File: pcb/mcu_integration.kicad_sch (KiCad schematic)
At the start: 32 parts, among them J5 DM3BT-DSF-PEJS, U1 STM32F103RBTx, U6 LM35DM, Y1 ECS-80-18-5PX-GM-TR

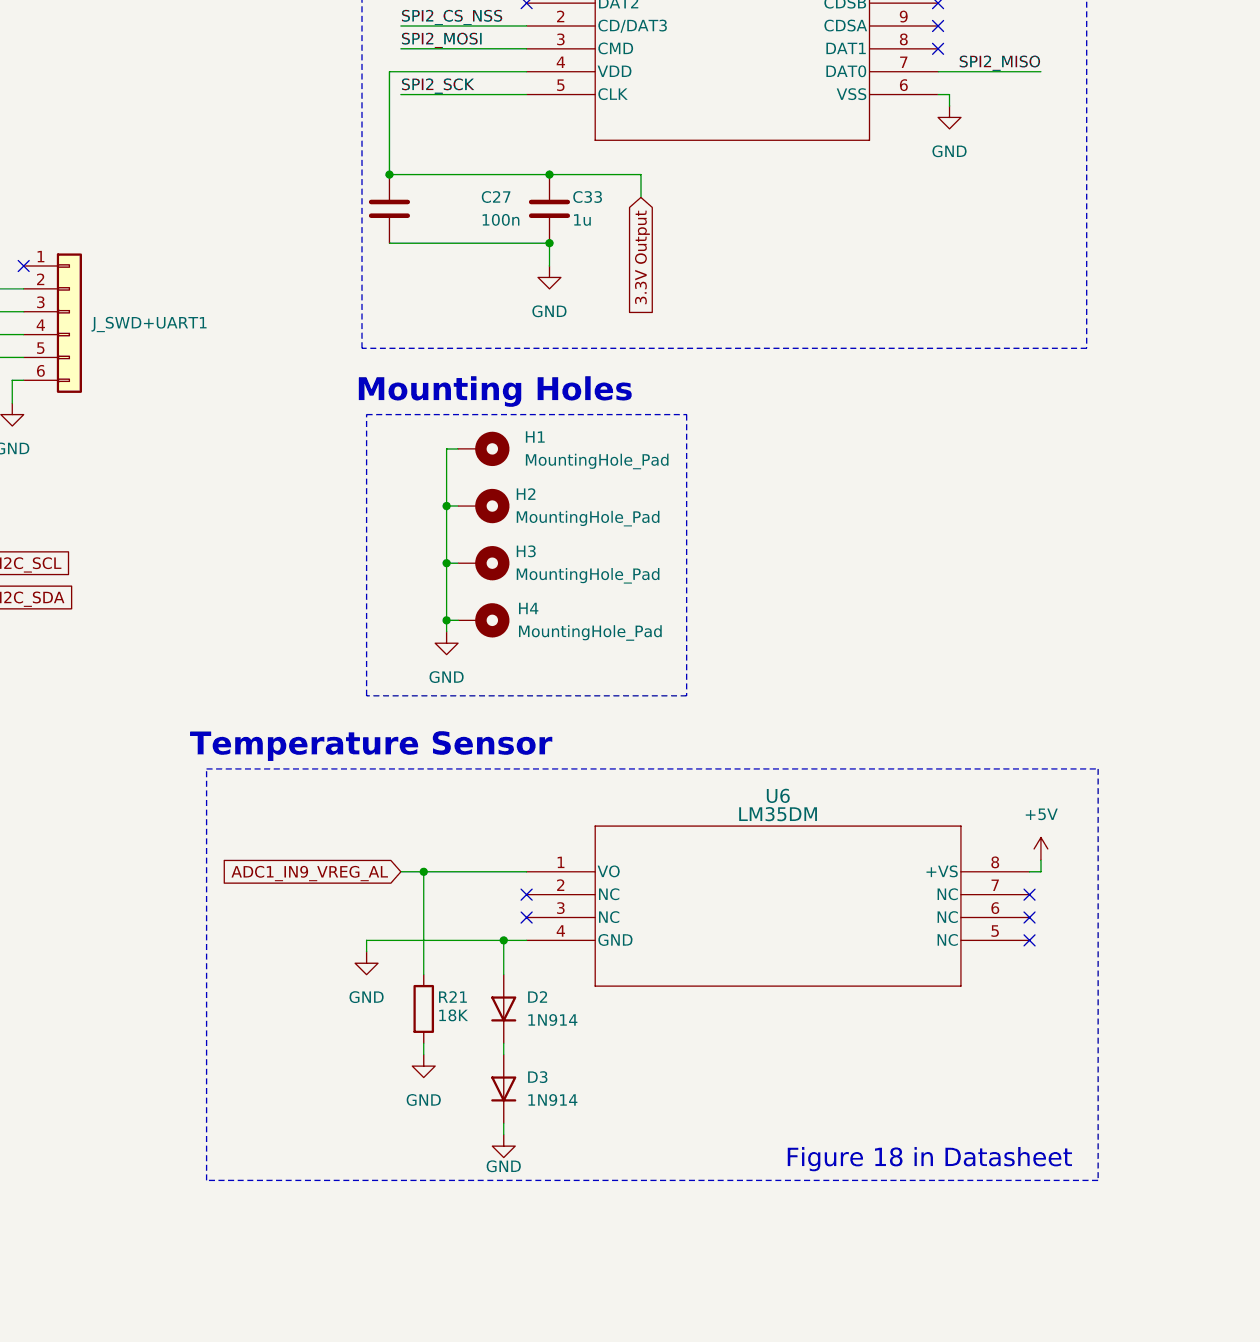
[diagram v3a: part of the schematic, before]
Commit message: Added GND and PWR planes
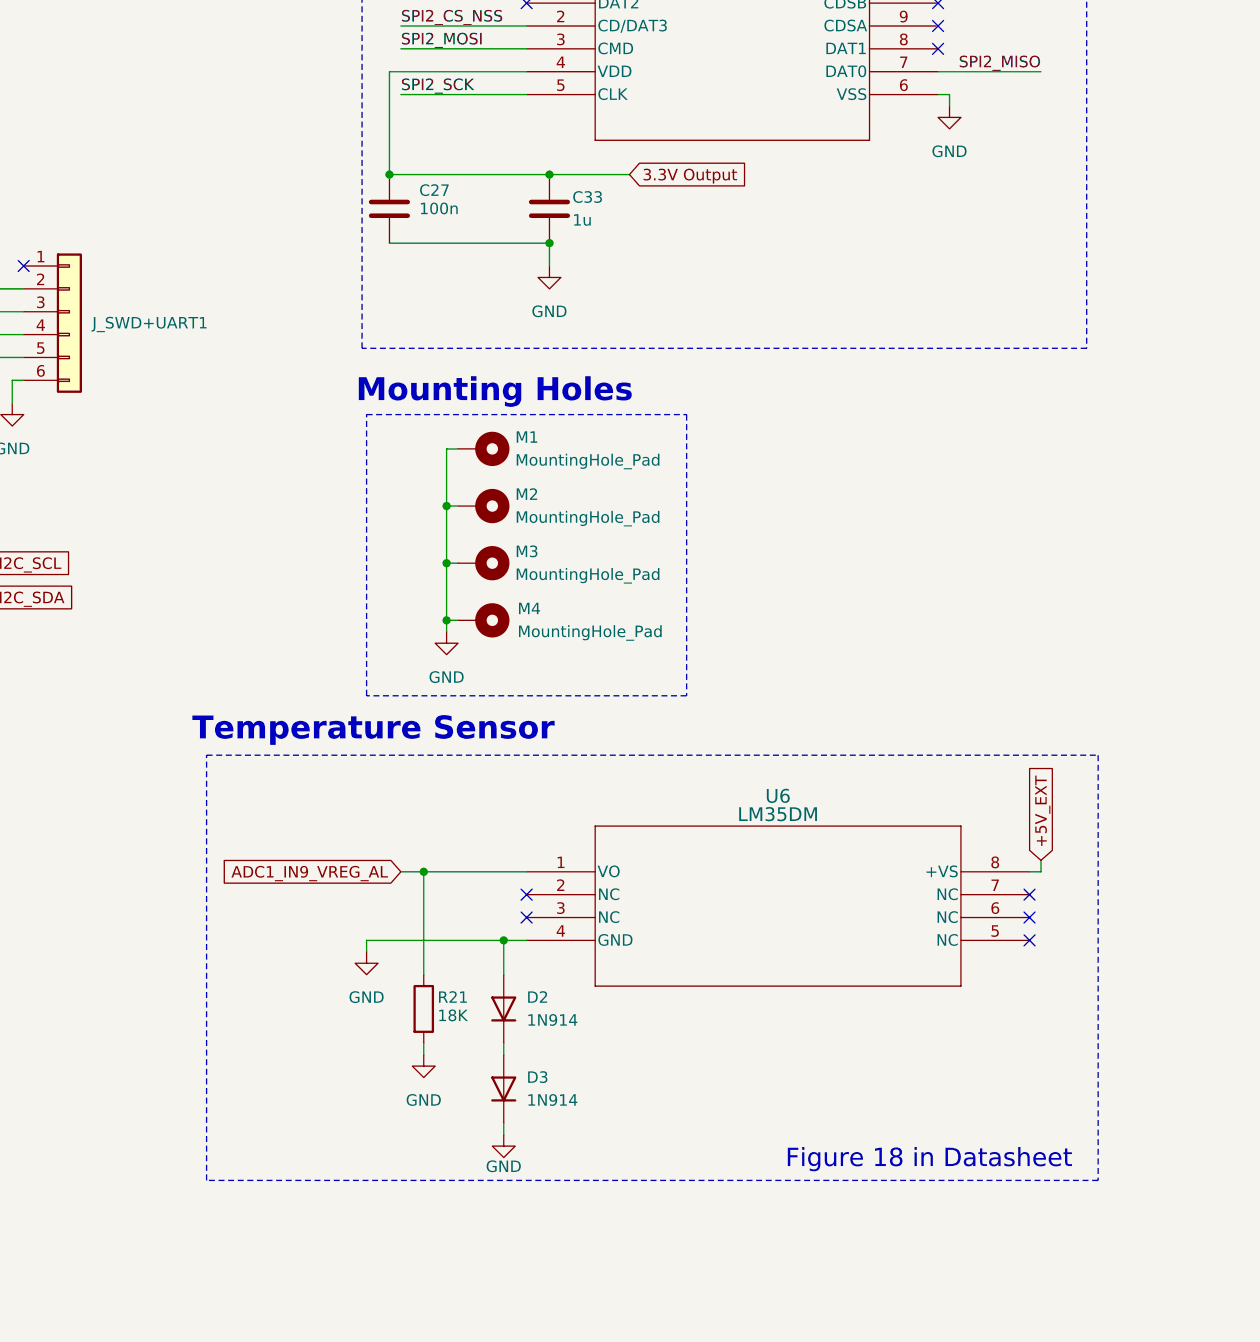
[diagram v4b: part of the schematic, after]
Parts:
- renumbered H1 to M1, H2 to M2, H3 to M3, H4 to M4
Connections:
- net +5V renamed +5V_EXT
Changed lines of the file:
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@@
 	(wire
 		(pts
-			(xy 232.41 54.61) (xy 232.41 52.07)
-		)
-		(stroke
-			(width 0)
-			(type default)
-		)
-	)
-	(wire
-		(pts
 			(xy 118.11 20.32) (xy 119.38 20.32)
 		)
@@
 	(wire
 		(pts
-			(xy 232.41 52.07) (xy 222.25 52.07)
+			(xy 231.14 52.07) (xy 222.25 52.07)
 		)
 		(stroke
@@
 	)
 	(rectangle
-		(start 184.15 118.11)
+		(start 184.15 116.586)
 		(end 283.21 163.83)
 		(stroke
@@
 	(text "Temperature Sensor"
 		(exclude_from_sim no)
-		(at 202.438 115.57 0)
+		(at 202.692 113.792 0)
 		(effects
 			(font
@@
 	(global_label "3.3V Output"
 		(shape input)
-		(at 232.41 54.61 270)
+		(at 231.14 52.07 0)
 		(fields_autoplaced yes)
 		(effects
@@
 				(size 1.27 1.27)
 			)
-			(justify right)
+			(justify left)
 		)
 		(property "Intersheetrefs" "${INTERSHEET_REFS}"
-			(at 232.41 68.9041 90)
+			(at 245.4341 52.07 0)
 			(effects
 				(font
 					(size 1.27 1.27)
 				)
-				(justify right)
+				(justify left)
 				(hide yes)
 			)
@@
 		)
 	)
+	(global_label "+5V_EXT"
+		(shape input)
+		(at 276.86 128.27 90)
+		(fields_autoplaced yes)
+		(effects
+			(font
+				(size 1.27 1.27)
+			)
+			(justify left)
+		)
+		(property "Intersheetrefs" "${INTERSHEET_REFS}"
+			(at 276.86 117.1206 90)
+			(effects
+				(font
+					(size 1.27 1.27)
+				)
+				(justify left)
+				(hide yes)
+			)
+		)
+	)
 	(global_label "ADC1_IN1_OPAMP_NOSHD"
 		(shape input)
@@
 		(on_board yes)
 		(dnp no)
-		(property "Reference" "H4"
+		(property "Reference" "M4"
 			(at 218.694 100.33 90)
 			(effects
@@
 			(project "mcu_integration"
 				(path "/c0210bc3-f67f-47d8-a34e-f002a728adb2"
-					(reference "H4")
+					(reference "M4")
 					(unit 1)
 				)
@@
 		(dnp no)
 		(fields_autoplaced yes)
-		(property "Reference" "H2"
+		(property "Reference" "M2"
 			(at 218.44 87.6299 90)
 			(effects
@@
 			(project "mcu_integration"
 				(path "/c0210bc3-f67f-47d8-a34e-f002a728adb2"
-					(reference "H2")
+					(reference "M2")
 					(unit 1)
 				)
@@
 		(dnp no)
 		(fields_autoplaced yes)
-		(property "Reference" "H3"
+		(property "Reference" "M3"
 			(at 218.44 93.9799 90)
 			(effects
@@
 			(project "mcu_integration"
 				(path "/c0210bc3-f67f-47d8-a34e-f002a728adb2"
-					(reference "H3")
+					(reference "M3")
 					(unit 1)
 				)
@@
 		(dnp no)
 		(property "Reference" "C27"
-			(at 214.63 54.61 0)
+			(at 207.772 53.848 0)
 			(effects
 				(font
@@
 		)
 		(property "Value" "100n"
-			(at 214.63 57.15 0)
+			(at 207.772 55.88 0)
 			(effects
 				(font
@@
 	)
 	(symbol
-		(lib_id "power:+5V")
-		(at 276.86 128.27 0)
-		(unit 1)
-		(exclude_from_sim no)
-		(in_bom yes)
-		(on_board yes)
-		(dnp no)
-		(fields_autoplaced yes)
-		(property "Reference" "#PWR079"
-			(at 276.86 132.08 0)
-			(effects
-				(font
-					(size 1.27 1.27)
-				)
-				(hide yes)
-			)
-		)
-		(property "Value" "+5V"
-			(at 276.86 123.19 0)
-			(effects
-				(font
-					(size 1.27 1.27)
-				)
-			)
-		)
-		(property "Footprint" ""
-			(at 276.86 128.27 0)
-			(effects
-				(font
-					(size 1.27 1.27)
-				)
-				(hide yes)
-			)
-		)
-		(property "Datasheet" ""
-			(at 276.86 128.27 0)
-			(effects
-				(font
-					(size 1.27 1.27)
-				)
-				(hide yes)
-			)
-		)
-		(property "Description" "Power symbol creates a global label with name \"+5V\""
-			(at 276.86 128.27 0)
-			(effects
-				(font
-					(size 1.27 1.27)
-				)
-				(hide yes)
-			)
-		)
-		(pin "1"
-		)
-		(instances
-			(project "mcu_integration"
-				(path "/c0210bc3-f67f-47d8-a34e-f002a728adb2"
-					(reference "#PWR079")
-					(unit 1)
-				)
-			)
-		)
-	)
-	(symbol
 		(lib_name "GND_1")
 		(lib_id "power:GND")
@@
 		(dnp no)
 		(fields_autoplaced yes)
-		(property "Reference" "H1"
-			(at 219.456 81.2799 90)
+		(property "Reference" "M1"
+			(at 218.44 81.2799 90)
 			(effects
 				(font
@@
 		)
 		(property "Value" "MountingHole_Pad"
-			(at 219.456 83.8199 90)
+			(at 218.44 83.8199 90)
 			(effects
 				(font
@@
 			(project "mcu_integration"
 				(path "/c0210bc3-f67f-47d8-a34e-f002a728adb2"
-					(reference "H1")
+					(reference "M1")
 					(unit 1)
 				)

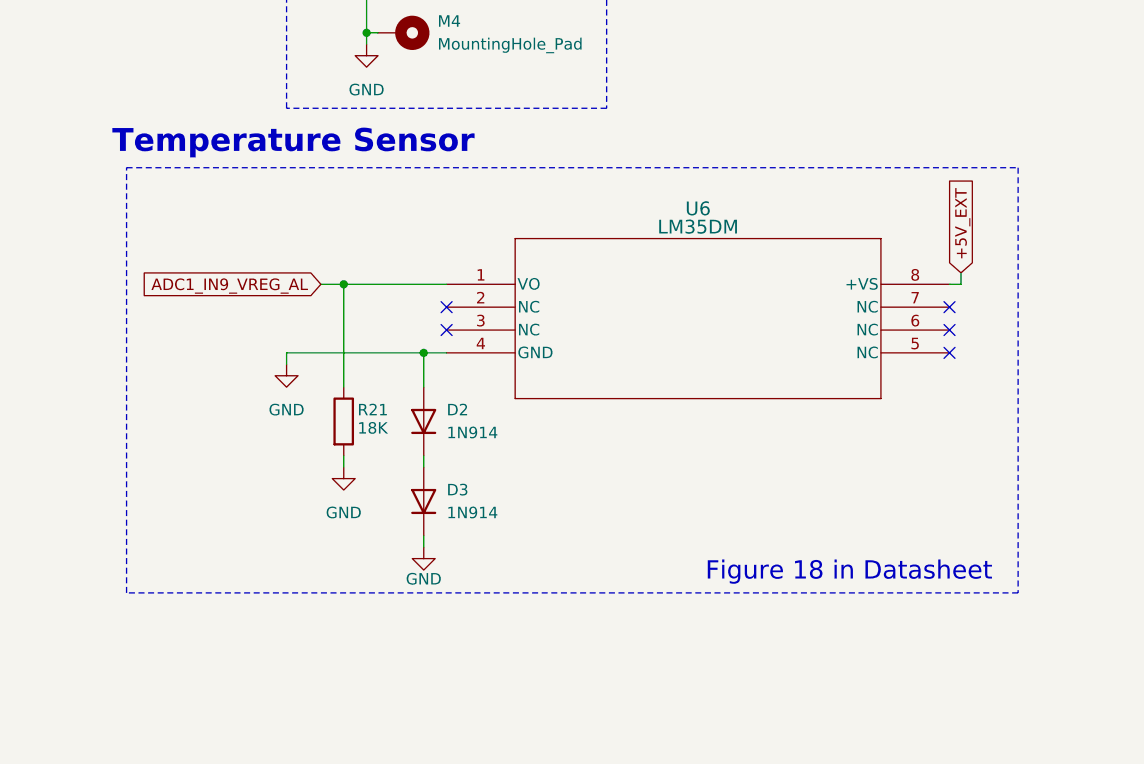
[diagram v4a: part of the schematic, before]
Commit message: Added +5v connections
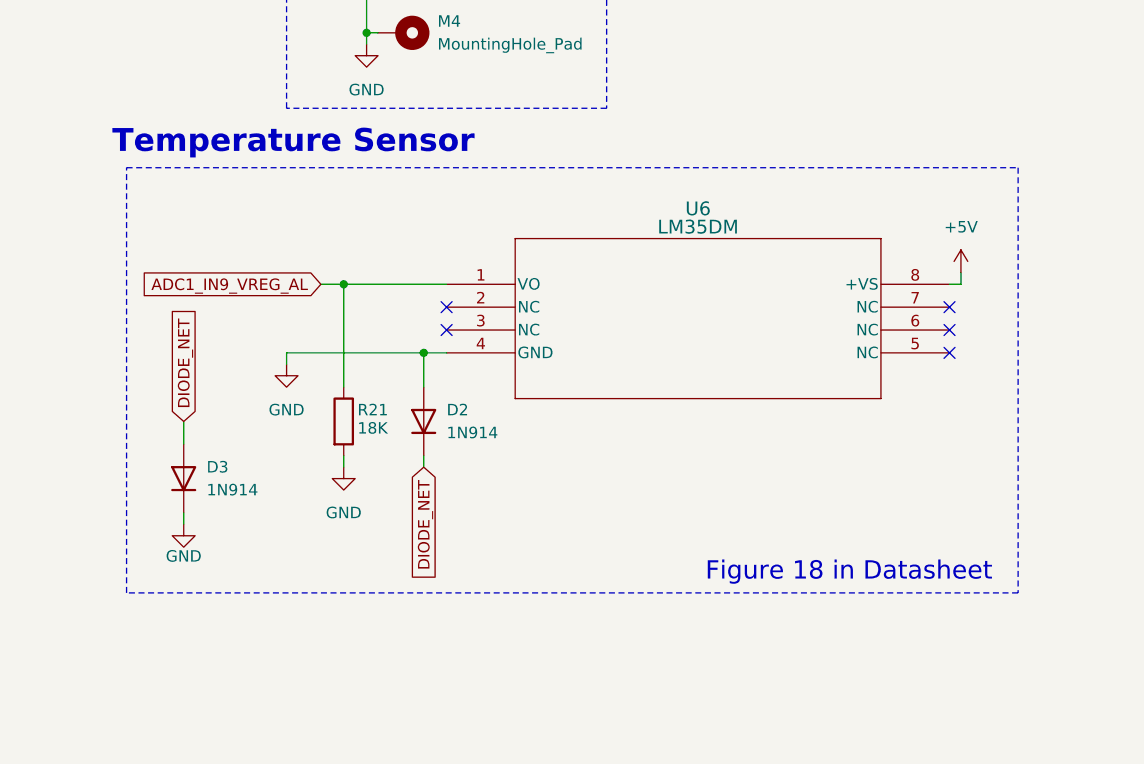
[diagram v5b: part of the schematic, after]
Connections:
- net DIODE_NET: now reaches D2.1 (K), D3.2 (A)
- net +5V_EXT renamed +5V
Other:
- moved on the sheet: D3
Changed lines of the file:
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@@
 	(wire
 		(pts
+			(xy 217.17 148.59) (xy 217.17 149.86)
+		)
+		(stroke
+			(width 0)
+			(type default)
+		)
+	)
+	(wire
+		(pts
 			(xy 106.68 21.59) (xy 118.11 21.59)
 		)
@@
 	(wire
 		(pts
+			(xy 190.5 144.78) (xy 190.5 147.32)
+		)
+		(stroke
+			(width 0)
+			(type default)
+		)
+	)
+	(wire
+		(pts
 			(xy 60.96 132.08) (xy 76.2 132.08)
 		)
@@
 	(wire
 		(pts
-			(xy 217.17 149.86) (xy 217.17 148.59)
-		)
-		(stroke
-			(width 0)
-			(type default)
-		)
-	)
-	(wire
-		(pts
 			(xy 205.74 38.1) (xy 219.71 38.1)
 		)
@@
 	(wire
 		(pts
-			(xy 217.17 157.48) (xy 217.17 158.75)
+			(xy 190.5 154.94) (xy 190.5 156.21)
 		)
 		(stroke
@@
 		)
 	)
+	(global_label "DIODE_NET"
+		(shape input)
+		(at 217.17 149.86 270)
+		(fields_autoplaced yes)
+		(effects
+			(font
+				(size 1.27 1.27)
+			)
+			(justify right)
+		)
+		(property "Intersheetrefs" "${INTERSHEET_REFS}"
+			(at 217.17 162.8842 90)
+			(effects
+				(font
+					(size 1.27 1.27)
+				)
+				(justify right)
+				(hide yes)
+			)
+		)
+	)
 	(global_label "ADC1_IN11_OPTO_E_NOSHD"
 		(shape input)
@@
 		)
 	)
-	(global_label "+5V_EXT"
+	(global_label "ADC1_IN1_OPAMP_NOSHD"
 		(shape input)
-		(at 276.86 128.27 90)
+		(at 127 39.37 0)
 		(fields_autoplaced yes)
 		(effects
@@
 		)
 		(property "Intersheetrefs" "${INTERSHEET_REFS}"
-			(at 276.86 117.1206 90)
+			(at 153.7524 39.37 0)
 			(effects
 				(font
@@
 		)
 	)
-	(global_label "ADC1_IN1_OPAMP_NOSHD"
+	(global_label "OBC_I2C_SCL"
 		(shape input)
-		(at 127 39.37 0)
+		(at 154.94 95.25 0)
 		(fields_autoplaced yes)
 		(effects
@@
 		)
 		(property "Intersheetrefs" "${INTERSHEET_REFS}"
-			(at 153.7524 39.37 0)
+			(at 170.3228 95.25 0)
 			(effects
 				(font
@@
 		)
 	)
-	(global_label "OBC_I2C_SCL"
+	(global_label "3.3V Output"
 		(shape input)
-		(at 154.94 95.25 0)
+		(at 93.98 15.24 180)
 		(fields_autoplaced yes)
 		(effects
@@
 				(size 1.27 1.27)
 			)
-			(justify left)
+			(justify right)
 		)
 		(property "Intersheetrefs" "${INTERSHEET_REFS}"
-			(at 170.3228 95.25 0)
+			(at 79.6859 15.24 0)
 			(effects
 				(font
 					(size 1.27 1.27)
 				)
-				(justify left)
+				(justify right)
 				(hide yes)
 			)
 		)
 	)
-	(global_label "3.3V Output"
+	(global_label "ADC1_IN5_VREF_MEL"
 		(shape input)
-		(at 93.98 15.24 180)
+		(at 127 49.53 0)
 		(fields_autoplaced yes)
 		(effects
@@
 				(size 1.27 1.27)
 			)
-			(justify right)
+			(justify left)
 		)
 		(property "Intersheetrefs" "${INTERSHEET_REFS}"
-			(at 79.6859 15.24 0)
+			(at 149.0956 49.53 0)
 			(effects
 				(font
 					(size 1.27 1.27)
 				)
-				(justify right)
+				(justify left)
 				(hide yes)
 			)
 		)
 	)
-	(global_label "ADC1_IN5_VREF_MEL"
+	(global_label "DIODE_NET"
 		(shape input)
-		(at 127 49.53 0)
+		(at 190.5 144.78 90)
 		(fields_autoplaced yes)
 		(effects
@@
 		)
 		(property "Intersheetrefs" "${INTERSHEET_REFS}"
-			(at 149.0956 49.53 0)
+			(at 190.5 131.7558 90)
 			(effects
 				(font
@@
 	)
 	(symbol
+		(lib_id "power:+5V")
+		(at 276.86 128.27 0)
+		(unit 1)
+		(exclude_from_sim no)
+		(in_bom yes)
+		(on_board yes)
+		(dnp no)
+		(fields_autoplaced yes)
+		(property "Reference" "#PWR079"
+			(at 276.86 132.08 0)
+			(effects
+				(font
+					(size 1.27 1.27)
+				)
+				(hide yes)
+			)
+		)
+		(property "Value" "+5V"
+			(at 276.86 123.19 0)
+			(effects
+				(font
+					(size 1.27 1.27)
+				)
+			)
+		)
+		(property "Footprint" ""
+			(at 276.86 128.27 0)
+			(effects
+				(font
+					(size 1.27 1.27)
+				)
+				(hide yes)
+			)
+		)
+		(property "Datasheet" ""
+			(at 276.86 128.27 0)
+			(effects
+				(font
+					(size 1.27 1.27)
+				)
+				(hide yes)
+			)
+		)
+		(property "Description" "Power symbol creates a global label with name \"+5V\""
+			(at 276.86 128.27 0)
+			(effects
+				(font
+					(size 1.27 1.27)
+				)
+				(hide yes)
+			)
+		)
+		(pin "1"
+		)
+		(instances
+			(project ""
+				(path "/c0210bc3-f67f-47d8-a34e-f002a728adb2"
+					(reference "#PWR079")
+					(unit 1)
+				)
+			)
+		)
+	)
+	(symbol
 		(lib_id "Device:FerriteBead")
 		(at 144.78 20.32 90)
@@
 		(lib_name "GND_3")
 		(lib_id "power:GND")
-		(at 217.17 158.75 0)
+		(at 190.5 156.21 0)
 		(unit 1)
 		(exclude_from_sim no)
@@
 		(dnp no)
 		(property "Reference" "#PWR078"
-			(at 217.17 165.1 0)
+			(at 190.5 162.56 0)
 			(effects
 				(font
@@
 		)
 		(property "Value" "GND"
-			(at 217.17 162.306 0)
+			(at 190.5 159.766 0)
 			(effects
 				(font
@@
 		)
 		(property "Footprint" ""
-			(at 217.17 158.75 0)
+			(at 190.5 156.21 0)
 			(effects
 				(font
@@
 		)
 		(property "Datasheet" ""
-			(at 217.17 158.75 0)
+			(at 190.5 156.21 0)
 			(effects
 				(font
@@
 		)
 		(property "Description" "Power symbol creates a global label with name \"GND\" , ground"
-			(at 217.17 158.75 0)
+			(at 190.5 156.21 0)
 			(effects
 				(font
@@
 	(symbol
 		(lib_id "Device:D")
-		(at 217.17 153.67 90)
+		(at 190.5 151.13 90)
 		(unit 1)
 		(exclude_from_sim no)
@@
 		(fields_autoplaced yes)
 		(property "Reference" "D3"
-			(at 219.71 152.3999 90)
+			(at 193.04 149.8599 90)
 			(effects
 				(font
@@
 		)
 		(property "Value" "1N914"
-			(at 219.71 154.9399 90)
+			(at 193.04 152.3999 90)
 			(effects
 				(font
@@
 		)
 		(property "Footprint" "Diode_SMD:D_0402_1005Metric"
-			(at 217.17 153.67 0)
+			(at 190.5 151.13 0)
 			(effects
 				(font
@@
 		)
 		(property "Datasheet" "~"
-			(at 217.17 153.67 0)
+			(at 190.5 151.13 0)
 			(effects
 				(font
@@
 		)
 		(property "Description" "Diode"
-			(at 217.17 153.67 0)
+			(at 190.5 151.13 0)
 			(effects
 				(font
@@
 		)
 		(property "Sim.Device" "D"
-			(at 217.17 153.67 0)
+			(at 190.5 151.13 0)
 			(effects
 				(font
@@
 		)
 		(property "Sim.Pins" "1=K 2=A"
-			(at 217.17 153.67 0)
+			(at 190.5 151.13 0)
 			(effects
 				(font

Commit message: Added silkscreen and changed diode footprints
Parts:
- D2, D3: footprint Diode_SMD:D_0402_1005Metric -> capstone:SOD-323_1P7X1P25_ONS
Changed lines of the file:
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@@
 	(label "SPI2_SCK"
 		(at 205.74 43.18 0)
-		(fields_autoplaced yes)
 		(effects
 			(font
@@
 	(label "SPI2_CS_NSS"
 		(at 205.74 35.56 0)
-		(fields_autoplaced yes)
 		(effects
 			(font
@@
 	(label "HSE_OSC_OUT"
 		(at 67.31 49.53 0)
-		(fields_autoplaced yes)
 		(effects
 			(font
@@
 	(label "USART1_TX"
 		(at 119.38 59.69 0)
-		(fields_autoplaced yes)
 		(effects
 			(font
@@
 	(label "HSE_OSC_IN"
 		(at 67.31 46.99 0)
-		(fields_autoplaced yes)
 		(effects
 			(font
@@
 	(label "SPI2_CS_NSS"
 		(at 119.38 110.49 0)
-		(fields_autoplaced yes)
 		(effects
 			(font
@@
 	(label "SPI2_MOSI"
 		(at 205.74 38.1 0)
-		(fields_autoplaced yes)
 		(effects
 			(font
@@
 	(label "SPI2_MOSI"
 		(at 119.38 118.11 0)
-		(fields_autoplaced yes)
 		(effects
 			(font
@@
 	(label "SPI2_MISO"
 		(at 119.38 115.57 0)
-		(fields_autoplaced yes)
 		(effects
 			(font
@@
 	(label "SWCLK"
 		(at 119.38 72.39 0)
-		(fields_autoplaced yes)
 		(effects
 			(font
@@
 	(label "USART1_RX"
 		(at 119.38 62.23 0)
-		(fields_autoplaced yes)
 		(effects
 			(font
@@
 	(label "SPI2_MISO"
 		(at 276.86 40.64 180)
-		(fields_autoplaced yes)
 		(effects
 			(font
@@
 	(label "BOOT0"
 		(at 68.58 40.64 0)
-		(fields_autoplaced yes)
 		(effects
 			(font
@@
 	(label "NRST"
 		(at 73.66 36.83 0)
-		(fields_autoplaced yes)
 		(effects
 			(font
@@
 	(label "SWDIO"
 		(at 119.38 69.85 0)
-		(fields_autoplaced yes)
 		(effects
 			(font
@@
 	(label "SPI2_SCK"
 		(at 119.38 113.03 0)
-		(fields_autoplaced yes)
 		(effects
 			(font
@@
 			)
 		)
-		(property "Footprint" "Diode_SMD:D_0402_1005Metric"
+		(property "Footprint" "capstone:SOD-323_1P7X1P25_ONS"
 			(at 217.17 144.78 0)
 			(effects
@@
 			)
 		)
-		(property "Footprint" "Diode_SMD:D_0402_1005Metric"
+		(property "Footprint" "capstone:SOD-323_1P7X1P25_ONS"
 			(at 190.5 151.13 0)
 			(effects
